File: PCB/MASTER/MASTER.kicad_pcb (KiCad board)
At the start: 2 copper layers, 13 parts, among them J1 Conn_01x02, J2 Conn_01x03, U1 NRF24L01_Breakout, U2 LM2596-Breakout-Board

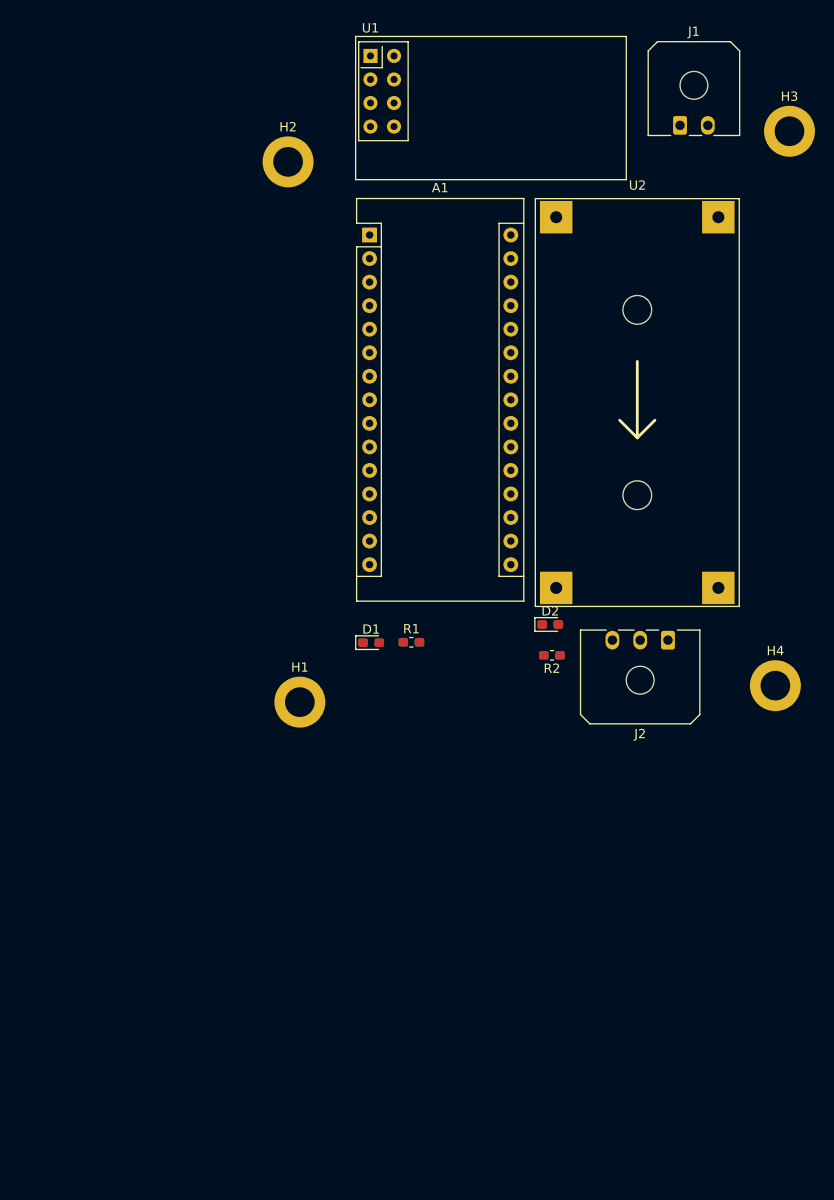
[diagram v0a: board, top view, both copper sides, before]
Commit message: Completed approximate layout. Need to route
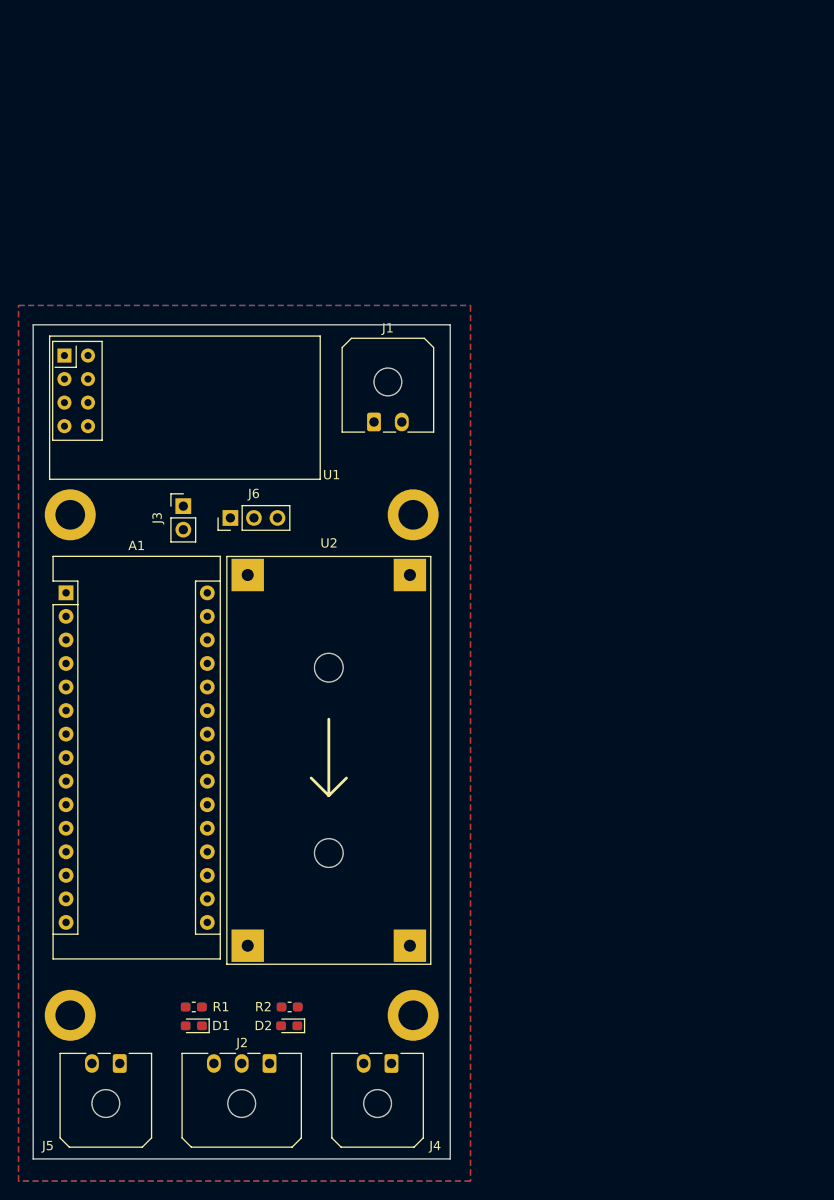
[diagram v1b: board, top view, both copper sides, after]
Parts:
- added J3: Conn_01x02, Connector_PinHeader_2.54mm:PinHeader_1x02_P2.54mm_Vertical, F.Cu at (76.2, 79.6)
- added J4: Conn_01x02, Connector_Molex:Molex_Micro-Fit_3.0_43650-0200_1x02_P3.00mm_Horizontal, F.Cu at (98.7, 139.7)
- added J5: Conn_01x02, Connector_Molex:Molex_Micro-Fit_3.0_43650-0200_1x02_P3.00mm_Horizontal, F.Cu at (69.3, 139.7)
- added J6: Conn_01x03, Connector_PinHeader_2.54mm:PinHeader_1x03_P2.54mm_Vertical, F.Cu at (81.3, 80.8)
- moved J2 62.7 mm to (85.5, 139.7)
- moved H3 58.0 mm to (101.0, 80.5)
- moved H4 52.8 mm to (101.0, 134.5)
- moved D2 51.7 mm to (87.6, 135.6), turned to 180 degrees
- moved U2 51.0 mm to (91.9, 107.0)
- moved A1 50.6 mm to (63.5, 88.9)
- moved R2 47.3 mm to (87.7, 133.6), turned to 0 degrees
- moved U1 46.2 mm to (63.4, 63.3)
- moved J1 46.0 mm to (96.8, 70.5)
- moved R1 45.8 mm to (77.3, 133.6)
- moved D1 45.6 mm to (77.3, 135.6), turned to 180 degrees
- moved H2 44.8 mm to (64.0, 80.5)
- moved H1 41.9 mm to (64.0, 134.5)
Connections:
- A1 pad 1: (no net) -> TX
- A1 pad 2: (no net) -> RX
- A1 pad 27: (no net) -> +5V
- A1 pad 6: (no net) -> D3
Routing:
- added copper zone on B.Cu, net GND
- added copper zone on F.Cu, net GND
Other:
- board outline added: 45 x 90 mm
- net class Default: trace_width 0.25 -> 0.381

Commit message: routed board
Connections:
- R1 pad 2: D9 -> D10
- R2 pad 2: D10 -> D9
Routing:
- net VCC: track 0.00 -> 104.0 mm
- net SCK: track 0.00 -> 73.7 mm
- net +3V3: track 0.00 -> 64.6 mm
- net MOSI: track 0.00 -> 59.1 mm
- net MISO: track 0.00 -> 55.7 mm
- net CSN: track 0.00 -> 53.2 mm
- net CE: track 0.00 -> 52.2 mm
- net D4: track 0.00 -> 45.5 mm
- net D3: track 0.00 -> 32.6 mm
- net D9: track 0.00 -> 32.2 mm
- net -BATT: track 0.00 -> 26.2 mm
- net +5V: track 0.00 -> 21.3 mm
- net D10: track 0.00 -> 20.9 mm
- net +BATT: track 0.00 -> 19.1 mm
- net TX: track 0.00 -> 17.2 mm
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
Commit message: MASTER review complete. Create gerbers
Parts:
- D1: value LED -> R-LED
- D2: value LED -> G-LED
- R1, R2: value R -> 220 ohm
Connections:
- R1 pad 2: D10 -> D9
- R2 pad 2: D9 -> D10
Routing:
- net D10: track 20.9 -> 38.5 mm
- net D9: track 32.2 -> 22.8 mm
- net GND: vias 0 -> 5
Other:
- board text added: "- + s"
- board text added: "Rx"
- board text added: "Tx"
- board text added: "V1.0"
- board text added: "Vin"
